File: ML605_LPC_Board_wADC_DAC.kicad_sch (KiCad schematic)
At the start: 19 parts, among them J1 ASP-134604-01, J10 Conn_02x06_Odd_Even, J11 Conn_02x06_Odd_Even, J12 Conn_02x06_Odd_Even, J2 Conn_01x03_Pin, J3 Conn_01x03_Pin, U1 LMV7219M7, U2 LMV7219M7, U3 NCV317

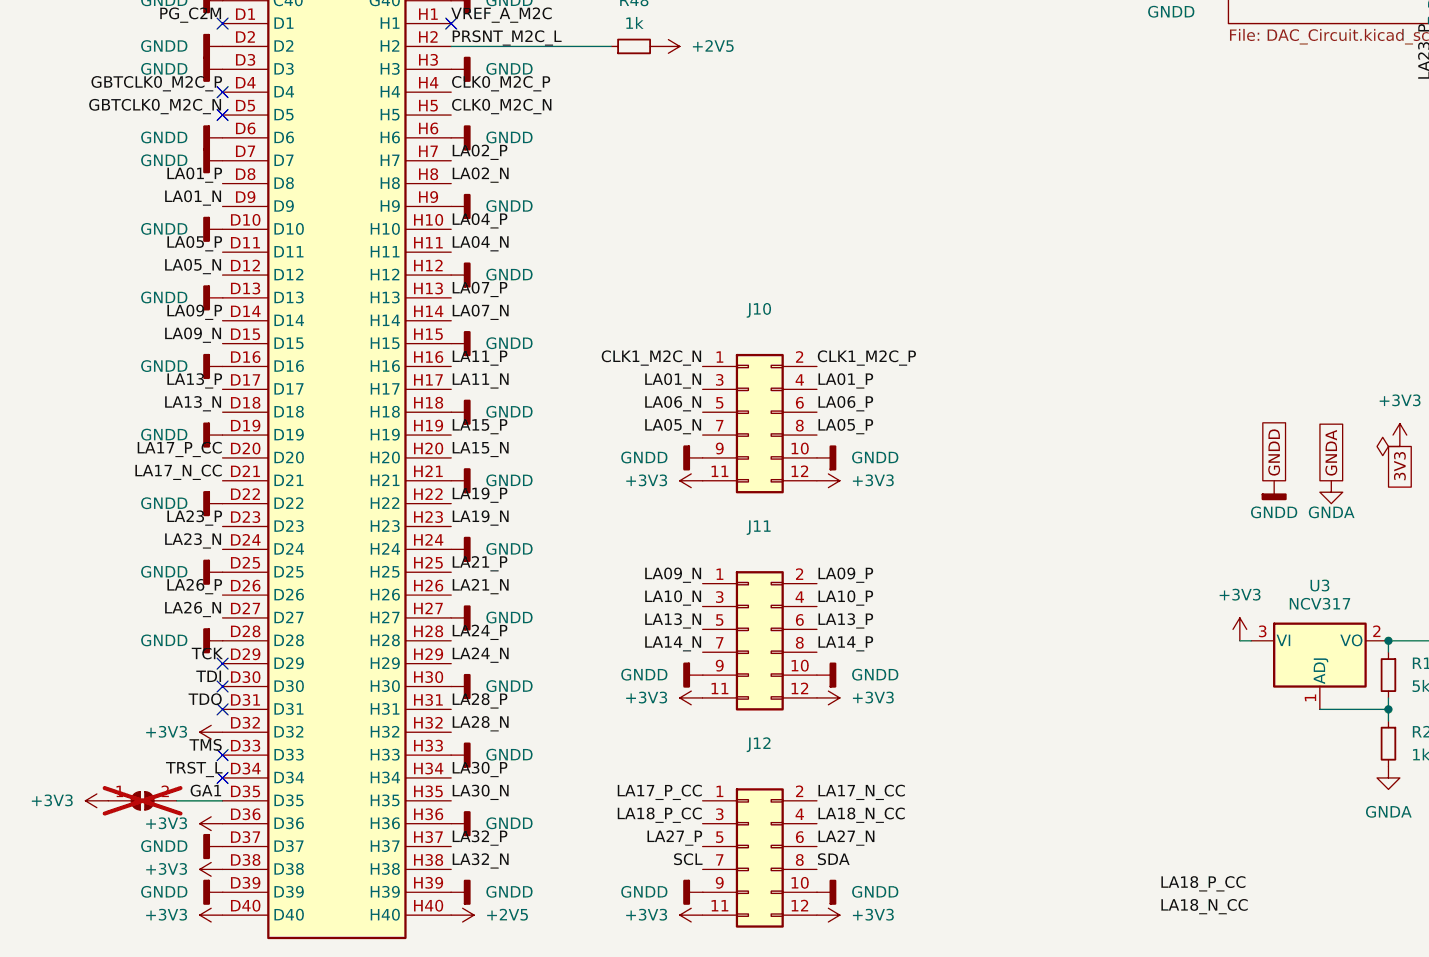
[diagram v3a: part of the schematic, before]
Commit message: Other minor changes
Including removing some unused nets in the schematic, changing L01_P/N back to L01_P/N_CC and adding the Mouser link to the BRD_PRSNT pullup resistor.
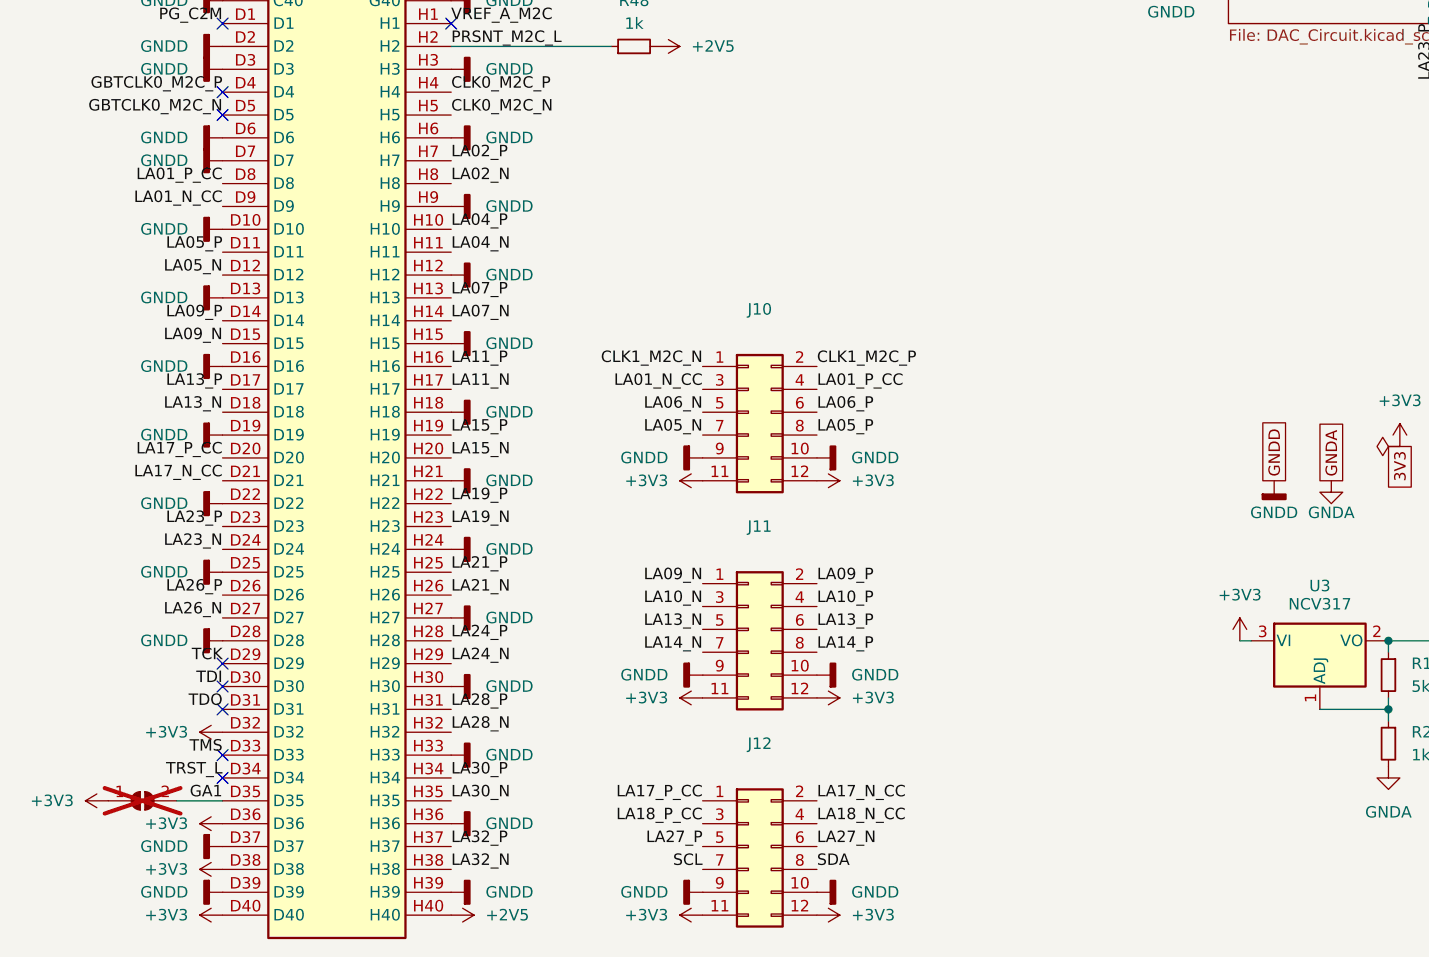
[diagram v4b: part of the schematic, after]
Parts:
- R48: Mouser Link (none) -> https://ro.mouser.com/ProductDetail/YAGEO/AC0805JR-071KL?qs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
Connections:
- net LA01_N renamed LA01_N_CC
- net LA01_P renamed LA01_P_CC
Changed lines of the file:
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@@
 		)
 	)
-	(label "LA01_N"
+	(label "LA01_N_CC"
 		(at 33.02 144.78 180)
 		(fields_autoplaced yes)
@@
 		)
 	)
-	(label "LA18_P_CC"
-		(at 137.16 220.98 0)
-		(fields_autoplaced yes)
-		(effects
-			(font
-				(size 1.27 1.27)
-			)
-			(justify left bottom)
-		)
-	)
 	(label "LA20_N"
 		(at 184.15 22.86 90)
@@
 		)
 	)
-	(label "LA01_N"
+	(label "LA01_N_CC"
 		(at 86.36 165.1 180)
 		(fields_autoplaced yes)
@@
 		)
 	)
-	(label "LA18_N_CC"
-		(at 137.16 223.52 0)
-		(fields_autoplaced yes)
-		(effects
-			(font
-				(size 1.27 1.27)
-			)
-			(justify left bottom)
-		)
-	)
 	(label "LA14_N"
 		(at 33.02 68.58 180)
@@
 		)
 	)
-	(label "LA01_P"
+	(label "LA01_P_CC"
 		(at 33.02 142.24 180)
 		(fields_autoplaced yes)
@@
 		)
 	)
-	(label "LA01_P"
+	(label "LA01_P_CC"
 		(at 99.06 165.1 0)
 		(fields_autoplaced yes)
@@
 			(at 78.74 127 0)
 			(effects
+				(font
+					(size 1.27 1.27)
+				)
+				(hide yes)
+			)
+		)
+		(property "Mouser Link" "https://ro.mouser.com/ProductDetail/YAGEO/AC0805JR-071KL?qs=sGAEpiMZZMtlubZbdhIBIG07xJe44c5APYMj%2Fj7aA%2Fo%3D"
+			(at 78.74 127 0)
+			(effects

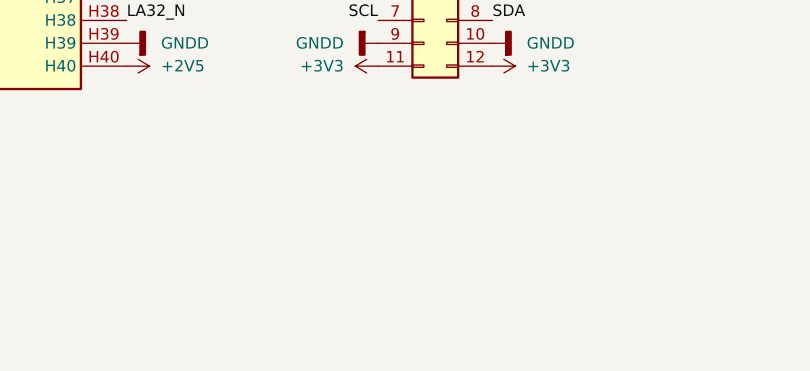
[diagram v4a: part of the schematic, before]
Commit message: Added GND stitching vias and fiducial markings
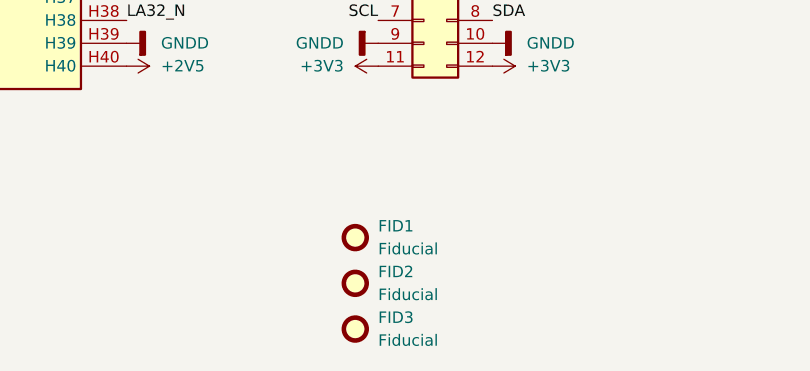
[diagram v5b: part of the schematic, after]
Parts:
- added FID1, FID2, FID3: Fiducial, Fiducial:Fiducial_0.5mm_Mask1mm, symbol Mechanical:Fiducial
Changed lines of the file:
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@@
+	)
+	(symbol
+		(lib_id "Mechanical:Fiducial")
+		(at 83.82 252.73 0)
+		(unit 1)
+		(exclude_from_sim yes)
+		(in_bom no)
+		(on_board yes)
+		(dnp no)
+		(fields_autoplaced yes)
+		(property "Reference" "FID3"
+			(at 86.36 251.4599 0)
+			(effects
+				(font
+					(size 1.27 1.27)
+				)
+				(justify left)
+			)
+		)
+		(property "Value" "Fiducial"
+			(at 86.36 253.9999 0)
+			(effects
+				(font
+					(size 1.27 1.27)
+				)
+				(justify left)
+			)
+		)
+		(property "Footprint" "Fiducial:Fiducial_0.5mm_Mask1mm"
+			(at 83.82 252.73 0)
+			(effects
+				(font
+					(size 1.27 1.27)
+				)
+				(hide yes)
+			)
+		)
+		(property "Datasheet" "~"
+			(at 83.82 252.73 0)
+			(effects
+				(font
+					(size 1.27 1.27)
+				)
+				(hide yes)
+			)
+		)
+		(property "Description" "Fiducial Marker"
+			(at 83.82 252.73 0)
+			(effects
+				(font
+					(size 1.27 1.27)
+				)
+				(hide yes)
+			)
+		)
+		(property "Mouser Link" "N/A"
+			(at 83.82 252.73 0)
+			(effects
+				(font
+					(size 1.27 1.27)
+				)
+				(hide yes)
+			)
+		)
+		(instances
+			(project ""
+				(path "/35bdcd8d-8b21-4a24-9357-7d92e5ad0993"
+					(reference "FID3")
+					(unit 1)
+				)
+			)
+		)
 	)
 	(symbol
@@
 	)
 	(symbol
+		(lib_id "Mechanical:Fiducial")
+		(at 83.82 247.65 0)
+		(unit 1)
+		(exclude_from_sim yes)
+		(in_bom no)
+		(on_board yes)
+		(dnp no)
+		(fields_autoplaced yes)
+		(property "Reference" "FID2"
+			(at 86.36 246.3799 0)
+			(effects
+				(font
+					(size 1.27 1.27)
+				)
+				(justify left)
+			)
+		)
+		(property "Value" "Fiducial"
+			(at 86.36 248.9199 0)
+			(effects
+				(font
+					(size 1.27 1.27)
+				)
+				(justify left)
+			)
+		)
+		(property "Footprint" "Fiducial:Fiducial_0.5mm_Mask1mm"
+			(at 83.82 247.65 0)
+			(effects
+				(font
+					(size 1.27 1.27)
+				)
+				(hide yes)
+			)
+		)
+		(property "Datasheet" "~"
+			(at 83.82 247.65 0)
+			(effects
+				(font
+					(size 1.27 1.27)
+				)
+				(hide yes)
+			)
+		)
+		(property "Description" "Fiducial Marker"
+			(at 83.82 247.65 0)
+			(effects
+				(font
+					(size 1.27 1.27)
+				)
+				(hide yes)
+			)
+		)
+		(property "Mouser Link" "N/A"
+			(at 83.82 247.65 0)
+			(effects
+				(font
+					(size 1.27 1.27)
+				)
+				(hide yes)
+			)
+		)
+		(instances
+			(project ""
+				(path "/35bdcd8d-8b21-4a24-9357-7d92e5ad0993"
+					(reference "FID2")
+					(unit 1)
+				)
+			)
+		)
+	)
+	(symbol
 		(lib_id "power:GNDD")
 		(at 33.02 91.44 270)
@@
 					(unit 1)
 				)
+			)
+		)
+	)
+	(symbol
+		(lib_id "Mechanical:Fiducial")
+		(at 83.82 242.57 0)
+		(unit 1)
+		(exclude_from_sim yes)
+		(in_bom no)
+		(on_board yes)
+		(dnp no)
+		(fields_autoplaced yes)
+		(property "Reference" "FID1"
+			(at 86.36 241.2999 0)
+			(effects
+				(font
+					(size 1.27 1.27)
+				)
+				(justify left)
+			)
+		)
+		(property "Value" "Fiducial"
+			(at 86.36 243.8399 0)
+			(effects
+				(font
+					(size 1.27 1.27)
+				)
+				(justify left)
+			)
+		)
+		(property "Footprint" "Fiducial:Fiducial_0.5mm_Mask1mm"
+			(at 83.82 242.57 0)
+			(effects
+				(font
+					(size 1.27 1.27)
+				)
+				(hide yes)
+			)
+		)
+		(property "Datasheet" "~"
+			(at 83.82 242.57 0)
+			(effects
+				(font
+					(size 1.27 1.27)
+				)
+				(hide yes)
+			)
+		)
+		(property "Description" "Fiducial Marker"
+			(at 83.82 242.57 0)
+			(effects
+				(font
+					(size 1.27 1.27)
+				)
+				(hide yes)
+			)
+		)
+		(property "Mouser Link" "N/A"
+			(at 83.82 242.57 0)
+			(effects
+				(font
+					(size 1.27 1.27)
+				)
+				(hide yes)
+			)
+		)
+		(instances
+			(project ""
+				(path "/35bdcd8d-8b21-4a24-9357-7d92e5ad0993"
+					(reference "FID1")
+					(unit 1)
+				)

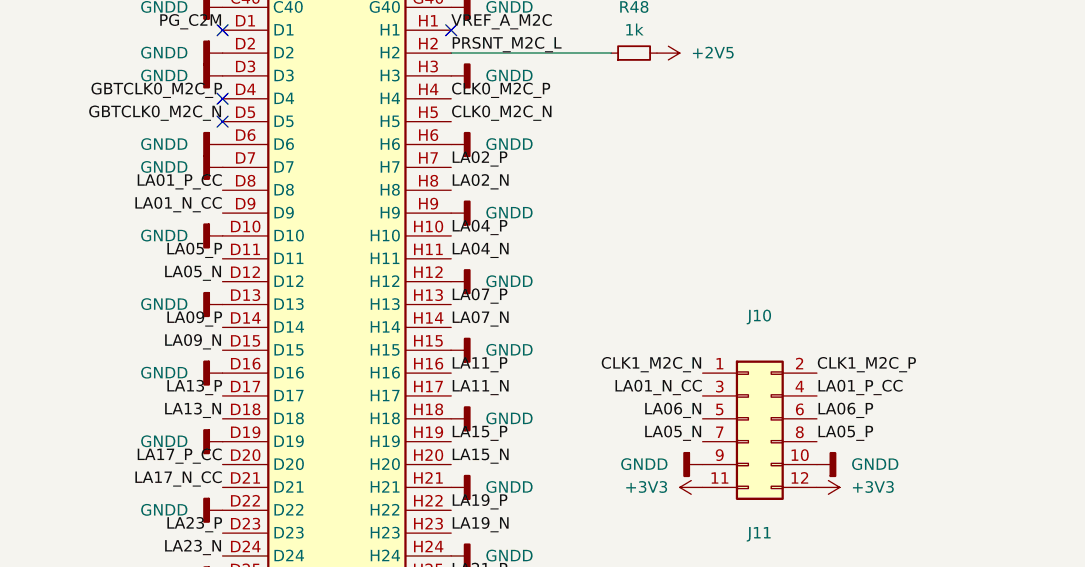
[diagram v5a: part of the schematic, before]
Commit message: Changed all via sizes to comply with the 0.2mm annular ring constraint
And fixed some other issues regarding clearance constraints
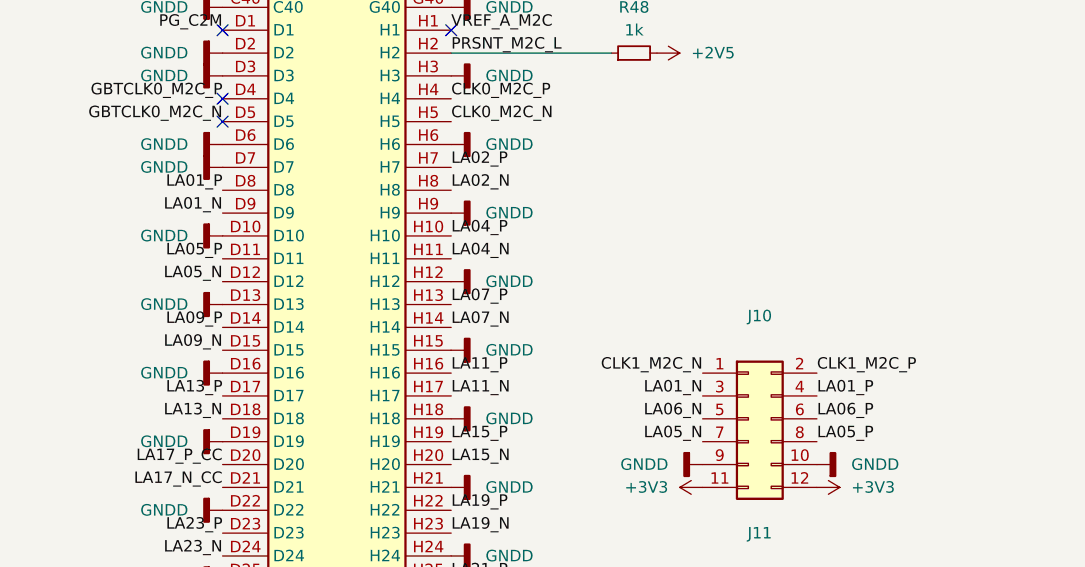
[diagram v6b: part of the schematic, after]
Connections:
- net LA01_N_CC renamed LA01_N
- net LA01_P_CC renamed LA01_P
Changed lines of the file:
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@@
 		)
 	)
-	(label "LA01_N_CC"
+	(label "LA01_N"
 		(at 33.02 144.78 180)
 		(fields_autoplaced yes)
@@
 		)
 	)
-	(label "LA01_N_CC"
+	(label "LA01_N"
 		(at 86.36 165.1 180)
 		(fields_autoplaced yes)
@@
 		)
 	)
-	(label "LA01_P_CC"
+	(label "LA01_P"
 		(at 33.02 142.24 180)
 		(fields_autoplaced yes)
@@
 		)
 	)
-	(label "LA01_P_CC"
+	(label "LA01_P"
 		(at 99.06 165.1 0)
 		(fields_autoplaced yes)
@@
 		)
 		(instances
-			(project ""
+			(project "ML605_LPC_Board_wADC_DAC"
 				(path "/35bdcd8d-8b21-4a24-9357-7d92e5ad0993"
 					(reference "FID3")
@@
 		)
 		(instances
-			(project ""
+			(project "ML605_LPC_Board_wADC_DAC"
 				(path "/35bdcd8d-8b21-4a24-9357-7d92e5ad0993"
 					(reference "FID2")
@@
 		)
 		(instances
-			(project ""
+			(project "ML605_LPC_Board_wADC_DAC"
 				(path "/35bdcd8d-8b21-4a24-9357-7d92e5ad0993"
 					(reference "FID1")

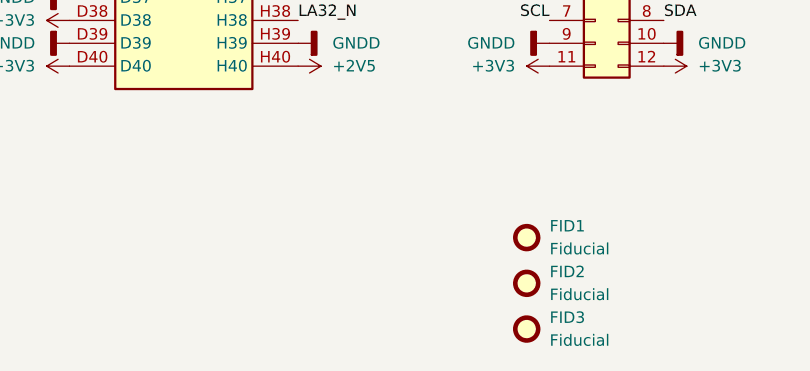
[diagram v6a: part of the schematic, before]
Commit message: Added fiducials on the back side of the PCB
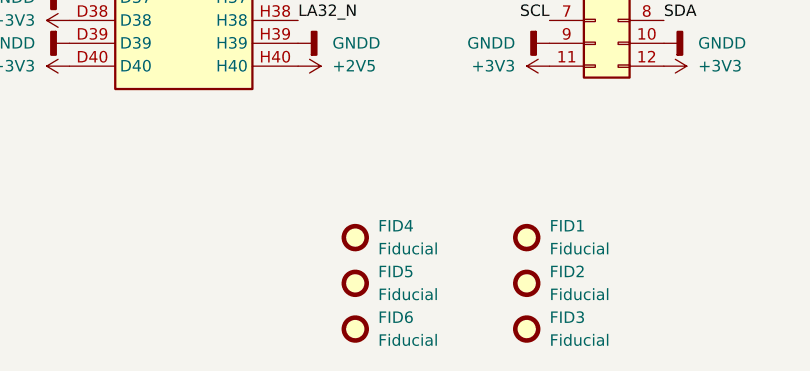
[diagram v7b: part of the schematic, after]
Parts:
- added FID4, FID5, FID6: Fiducial, Fiducial:Fiducial_0.5mm_Mask1mm, symbol Mechanical:Fiducial
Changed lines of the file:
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@@
 	)
 	(symbol
+		(lib_id "Mechanical:Fiducial")
+		(at 64.77 252.73 0)
+		(unit 1)
+		(exclude_from_sim yes)
+		(in_bom no)
+		(on_board yes)
+		(dnp no)
+		(fields_autoplaced yes)
+		(property "Reference" "FID6"
+			(at 67.31 251.4599 0)
+			(effects
+				(font
+					(size 1.27 1.27)
+				)
+				(justify left)
+			)
+		)
+		(property "Value" "Fiducial"
+			(at 67.31 253.9999 0)
+			(effects
+				(font
+					(size 1.27 1.27)
+				)
+				(justify left)
+			)
+		)
+		(property "Footprint" "Fiducial:Fiducial_0.5mm_Mask1mm"
+			(at 64.77 252.73 0)
+			(effects
+				(font
+					(size 1.27 1.27)
+				)
+				(hide yes)
+			)
+		)
+		(property "Datasheet" "~"
+			(at 64.77 252.73 0)
+			(effects
+				(font
+					(size 1.27 1.27)
+				)
+				(hide yes)
+			)
+		)
+		(property "Description" "Fiducial Marker"
+			(at 64.77 252.73 0)
+			(effects
+				(font
+					(size 1.27 1.27)
+				)
+				(hide yes)
+			)
+		)
+		(property "Mouser Link" "N/A"
+			(at 64.77 252.73 0)
+			(effects
+				(font
+					(size 1.27 1.27)
+				)
+				(hide yes)
+			)
+		)
+		(instances
+			(project "ML605_LPC_Board_wADC_DAC"
+				(path "/35bdcd8d-8b21-4a24-9357-7d92e5ad0993"
+					(reference "FID6")
+					(unit 1)
+				)
+			)
+		)
+	)
+	(symbol
 		(lib_id "power:GNDD")
 		(at 58.42 93.98 90)
@@
 	)
 	(symbol
+		(lib_id "Mechanical:Fiducial")
+		(at 64.77 242.57 0)
+		(unit 1)
+		(exclude_from_sim yes)
+		(in_bom no)
+		(on_board yes)
+		(dnp no)
+		(fields_autoplaced yes)
+		(property "Reference" "FID4"
+			(at 67.31 241.2999 0)
+			(effects
+				(font
+					(size 1.27 1.27)
+				)
+				(justify left)
+			)
+		)
+		(property "Value" "Fiducial"
+			(at 67.31 243.8399 0)
+			(effects
+				(font
+					(size 1.27 1.27)
+				)
+				(justify left)
+			)
+		)
+		(property "Footprint" "Fiducial:Fiducial_0.5mm_Mask1mm"
+			(at 64.77 242.57 0)
+			(effects
+				(font
+					(size 1.27 1.27)
+				)
+				(hide yes)
+			)
+		)
+		(property "Datasheet" "~"
+			(at 64.77 242.57 0)
+			(effects
+				(font
+					(size 1.27 1.27)
+				)
+				(hide yes)
+			)
+		)
+		(property "Description" "Fiducial Marker"
+			(at 64.77 242.57 0)
+			(effects
+				(font
+					(size 1.27 1.27)
+				)
+				(hide yes)
+			)
+		)
+		(property "Mouser Link" "N/A"
+			(at 64.77 242.57 0)
+			(effects
+				(font
+					(size 1.27 1.27)
+				)
+				(hide yes)
+			)
+		)
+		(instances
+			(project "ML605_LPC_Board_wADC_DAC"
+				(path "/35bdcd8d-8b21-4a24-9357-7d92e5ad0993"
+					(reference "FID4")
+					(unit 1)
+				)
+			)
+		)
+	)
+	(symbol
 		(lib_id "power:GNDD")
 		(at 58.42 71.12 90)
@@
 					(unit 1)
 				)
+			)
+		)
+	)
+	(symbol
+		(lib_id "Mechanical:Fiducial")
+		(at 64.77 247.65 0)
+		(unit 1)
+		(exclude_from_sim yes)
+		(in_bom no)
+		(on_board yes)
+		(dnp no)
+		(fields_autoplaced yes)
+		(property "Reference" "FID5"
+			(at 67.31 246.3799 0)
+			(effects
+				(font
+					(size 1.27 1.27)
+				)
+				(justify left)
+			)
+		)
+		(property "Value" "Fiducial"
+			(at 67.31 248.9199 0)
+			(effects
+				(font
+					(size 1.27 1.27)
+				)
+				(justify left)
+			)
+		)
+		(property "Footprint" "Fiducial:Fiducial_0.5mm_Mask1mm"
+			(at 64.77 247.65 0)
+			(effects
+				(font
+					(size 1.27 1.27)
+				)
+				(hide yes)
+			)
+		)
+		(property "Datasheet" "~"
+			(at 64.77 247.65 0)
+			(effects
+				(font
+					(size 1.27 1.27)
+				)
+				(hide yes)
+			)
+		)
+		(property "Description" "Fiducial Marker"
+			(at 64.77 247.65 0)
+			(effects
+				(font
+					(size 1.27 1.27)
+				)
+				(hide yes)
+			)
+		)
+		(property "Mouser Link" "N/A"
+			(at 64.77 247.65 0)
+			(effects
+				(font
+					(size 1.27 1.27)
+				)
+				(hide yes)
+			)
+		)
+		(instances
+			(project "ML605_LPC_Board_wADC_DAC"
+				(path "/35bdcd8d-8b21-4a24-9357-7d92e5ad0993"
+					(reference "FID5")
+					(unit 1)
+				)

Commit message: Added BOM
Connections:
- net LA01_N renamed LA01_N_CC
- net LA01_P renamed LA01_P_CC
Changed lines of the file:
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@@
 		)
 	)
-	(label "LA01_N"
+	(label "LA01_N_CC"
 		(at 33.02 144.78 180)
 		(fields_autoplaced yes)
@@
 		)
 	)
-	(label "LA01_N"
+	(label "LA01_N_CC"
 		(at 86.36 165.1 180)
 		(fields_autoplaced yes)
@@
 		)
 	)
-	(label "LA01_P"
+	(label "LA01_P_CC"
 		(at 33.02 142.24 180)
 		(fields_autoplaced yes)
@@
 		)
 	)
-	(label "LA01_P"
+	(label "LA01_P_CC"
 		(at 99.06 165.1 0)
 		(fields_autoplaced yes)
